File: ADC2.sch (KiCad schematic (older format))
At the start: 11 parts, among them U36 TLA2024IRUGR

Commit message: PVT
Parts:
- U56: renamed from U36; value TLA2024IRUGR -> ADS1015IDGSR; footprint IC-QFN:QFN10_1.5x2.0_P0.5_001 -> IC-SOP:VSSOP10_3.0x3.0_P0.5; symbol analog-ti:TLA2024 -> analog-ti:ADS1015; PartName TLA2024IRUGR -> ADS1015IDGSR
- renumbered C154 to C231, C155 to C232, C156 to C233, R92 to R119, R93 to R120, R94 to R121, R95 to R122, R96 to R123, TP31 to TP29, TP32 to TP30
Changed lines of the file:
@@
 $Descr A4 11693 8268
 encoding utf-8
-Sheet 18 24
-Title "Phoenix DVT"
-Date "2020-05-18"
+Sheet 24 24
+Title "Phoenix PVT"
+Date "2020-07-19"
 Rev "1"
 Comp ""
@@
 $EndDescr
 $Comp
-L analog-ti:TLA2024 U36
+L analog-ti:ADS1015 U56
 U 1 1 5E49C93C
 P 6000 4000
-F 0 "U36" H 6000 4650 50  0000 C CNN
-F 1 "TLA2024IRUGR" H 6000 3350 50  0000 C CNN
-F 2 "IC-QFN:QFN10_1.5x2.0_P0.5_001" H 6000 4000 50  0001 C CNN
+F 0 "U56" H 6000 4650 50  0000 C CNN
+F 1 "ADS1015IDGSR" H 6000 3350 50  0000 C CNN
+F 2 "IC-SOP:VSSOP10_3.0x3.0_P0.5" H 6000 4000 50  0001 C CNN
 F 3 "" H 6000 4000 50  0001 C CNN
-F 4 "TLA2024IRUGR" H 6000 4000 50  0001 C CNN "PartName"
+F 4 "ADS1015IDGSR" H 6000 4000 50  0001 C CNN "PartName"
 	1    6000 4000
 	1    0    0    -1
 $EndComp
 $Comp
-L passive:C C154
+L passive:C C231
 U 1 1 5E49D189
 P 5400 3700
-F 0 "C154" H 5500 3750 50  0000 L CNN
+F 0 "C231" H 5500 3750 50  0000 L CNN
 F 1 "100n" H 5500 3650 50  0000 L CNN
 F 2 "Capacitor-Chip:C_CHIP_1005_Hand_NoSilk" H 5500 3600 50  0001 C CNN
@@
 	7000 3400 7000 3700
 $Comp
-L supply-value:+3V3 #PWR0315
+L supply-value:+3V3 #PWR0438
 U 1 1 5E49DFE0
 P 6600 3200
-F 0 "#PWR0315" H 6600 3050 50  0001 C CNN
+F 0 "#PWR0438" H 6600 3050 50  0001 C CNN
 F 1 "+3V3" H 6600 3340 50  0000 C CNN
 F 2 "" H 6600 3200 50  0001 C CNN
@@
 $EndComp
 $Comp
-L supply-value:+3V3 #PWR0317
+L supply-value:+3V3 #PWR0440
 U 1 1 5E49E481
 P 7000 3200
-F 0 "#PWR0317" H 7000 3050 50  0001 C CNN
+F 0 "#PWR0440" H 7000 3050 50  0001 C CNN
 F 1 "+3V3" H 7000 3340 50  0000 C CNN
 F 2 "" H 7000 3200 50  0001 C CNN
@@
 $EndComp
 $Comp
-L supply-alias:GND #PWR0313
+L supply-alias:GND #PWR0436
 U 1 1 5E49E826
 P 5400 3900
-F 0 "#PWR0313" H 5400 3650 50  0001 C CNN
+F 0 "#PWR0436" H 5400 3650 50  0001 C CNN
 F 1 "GND" H 5400 3750 50  0000 C CNN
 F 2 "" H 5400 3900 50  0001 C CNN
@@
 	5400 3500 5600 3500
 $Comp
-L supply-alias:GND #PWR0314
+L supply-alias:GND #PWR0437
 U 1 1 5E4A0461
 P 5400 4500
-F 0 "#PWR0314" H 5400 4250 50  0001 C CNN
+F 0 "#PWR0437" H 5400 4250 50  0001 C CNN
 F 1 "GND" H 5400 4350 50  0000 C CNN
 F 2 "" H 5400 4500 50  0001 C CNN
@@
 CS-
 $Comp
-L supply-alias:GND #PWR0318
+L supply-alias:GND #PWR0441
 U 1 1 5E4A21A6
 P 7000 4900
-F 0 "#PWR0318" H 7000 4650 50  0001 C CNN
+F 0 "#PWR0441" H 7000 4650 50  0001 C CNN
 F 1 "GND" H 7000 4750 50  0000 C CNN
 F 2 "" H 7000 4900 50  0001 C CNN
@@
 	7400 4500 7400 4600
 $Comp
-L passive:C C155
+L passive:C C232
 U 1 1 5E4A2C50
 P 7000 4700
-F 0 "C155" H 7100 4750 50  0000 L CNN
+F 0 "C232" H 7100 4750 50  0000 L CNN
 F 1 "10n" H 7100 4650 50  0000 L CNN
 F 2 "Capacitor-Chip:C_CHIP_1005_Hand_NoSilk" H 7100 4600 50  0001 C CNN
@@
 $EndComp
 $Comp
-L passive:R R95
+L passive:R R122
 U 1 1 5E4A13E8
 P 7900 4500
-F 0 "R95" V 7800 4500 50  0000 C CNN
+F 0 "R122" V 7800 4500 50  0000 C CNN
 F 1 "100k" V 8000 4500 50  0000 C CNN
 F 2 "Resistor-Chip:R_CHIP_1005_Hand_NoSilk" V 7950 4400 50  0001 C CNN
@@
 $EndComp
 $Comp
-L supply-value:+48V #PWR0319
+L supply-value:+48V #PWR0442
 U 1 1 5E4A0E38
 P 8700 4500
-F 0 "#PWR0319" H 8700 4350 50  0001 C CNN
+F 0 "#PWR0442" H 8700 4350 50  0001 C CNN
 F 1 "+48V" H 8700 4640 50  0000 C CNN
 F 2 "" H 8700 4500 50  0001 C CNN
@@
 Connection ~ 7000 4900
 $Comp
-L passive:R R94
+L passive:R R121
 U 1 1 5E4A1DE3
 P 7400 4700
-F 0 "R94" H 7450 4750 50  0000 L CNN
+F 0 "R121" H 7450 4750 50  0000 L CNN
 F 1 "10k" H 7450 4650 50  0000 L CNN
 F 2 "Resistor-Chip:R_CHIP_1005_Hand_NoSilk" V 7450 4600 50  0001 C CNN
@@
 SDA
 $Comp
-L passive:C C156
+L passive:C C233
 U 1 1 5E5FCC2A
 P 7600 4000
-F 0 "C156" H 7700 4050 50  0000 L CNN
+F 0 "C233" H 7700 4050 50  0000 L CNN
 F 1 "100n" H 7700 3950 50  0000 L CNN
 F 2 "Capacitor-Chip:C_CHIP_1005_Hand_NoSilk" H 7700 3900 50  0001 C CNN
@@
 	6400 4100 7600 4100
 $Comp
-L passive:R R96
+L passive:R R123
 U 1 1 5F388480
 P 8400 4500
-F 0 "R96" V 8300 4500 50  0000 C CNN
+F 0 "R123" V 8300 4500 50  0000 C CNN
 F 1 "100k" V 8500 4500 50  0000 C CNN
 F 2 "Resistor-Chip:R_CHIP_1005_Hand_NoSilk" V 8450 4400 50  0001 C CNN
@@
 	6400 3900 7600 3900
 $Comp
-L supply-value:+3V3 #PWR0312
+L supply-value:+3V3 #PWR0435
 U 1 1 5EE44233
 P 5400 3500
-F 0 "#PWR0312" H 5400 3350 50  0001 C CNN
+F 0 "#PWR0435" H 5400 3350 50  0001 C CNN
 F 1 "+3V3" H 5400 3640 50  0000 C CNN
 F 2 "" H 5400 3500 50  0001 C CNN
@@
 Connection ~ 5400 3500
 $Comp
-L supply-alias:GND #PWR0316
+L supply-alias:GND #PWR0439
 U 1 1 5EEE5CDA
 P 6600 4500
-F 0 "#PWR0316" H 6600 4250 50  0001 C CNN
+F 0 "#PWR0439" H 6600 4250 50  0001 C CNN
 F 1 "GND" H 6600 4350 50  0000 C CNN
 F 2 "" H 6600 4500 50  0001 C CNN
@@
 	6400 3700 7000 3700
 $Comp
-L passive:R R92
+L passive:R R119
 U 1 1 5ED19405
 P 6600 3300
-F 0 "R92" H 6650 3350 50  0000 L CNN
+F 0 "R119" H 6650 3350 50  0000 L CNN
 F 1 "4.7k" H 6650 3250 50  0000 L CNN
 F 2 "Resistor-Chip:R_CHIP_1005_Hand_NoSilk" V 6650 3200 50  0001 C CNN
@@
 $EndComp
 $Comp
-L passive:R R93
+L passive:R R120
 U 1 1 5ED19765
 P 7000 3300
-F 0 "R93" H 7050 3350 50  0000 L CNN
+F 0 "R120" H 7050 3350 50  0000 L CNN
 F 1 "4.7k" H 7050 3250 50  0000 L CNN
 F 2 "Resistor-Chip:R_CHIP_1005_Hand_NoSilk" V 7050 3200 50  0001 C CNN
@@
 $EndComp
 $Comp
-L print:TestPoint TP31
+L print:TestPoint TP29
 U 1 1 5EF086EC
 P 7400 3400
-F 0 "TP31" H 7400 3700 50  0000 C CNN
+F 0 "TP29" H 7400 3700 50  0000 C CNN
 F 1 "SCL" H 7400 3600 50  0000 C CNN
 F 2 "Print:TP_C0.8" H 7100 3650 50  0001 C CNN
@@
 $EndComp
 $Comp
-L print:TestPoint TP32
+L print:TestPoint TP30
 U 1 1 5EF08F12
 P 7800 3400
-F 0 "TP32" H 7800 3700 50  0000 C CNN
+F 0 "TP30" H 7800 3700 50  0000 C CNN
 F 1 "SDA" H 7800 3600 50  0000 C CNN
 F 2 "Print:TP_C0.8" H 7500 3650 50  0001 C CNN

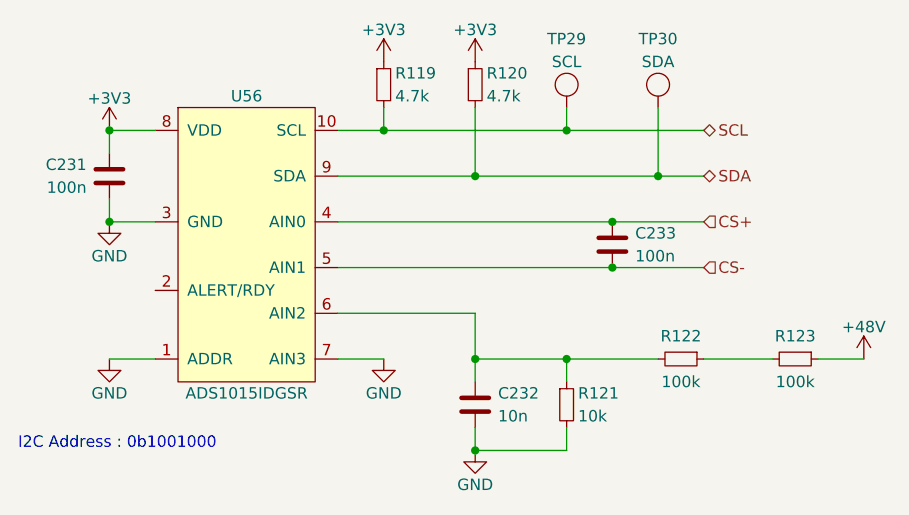
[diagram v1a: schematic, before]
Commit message: SBUにTVSダイオードを追加
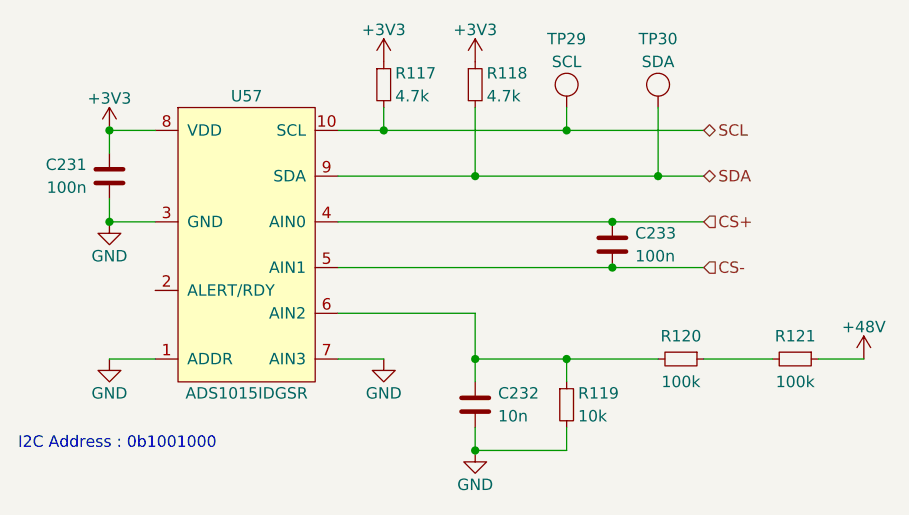
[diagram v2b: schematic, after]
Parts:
- renumbered R119 to R117, R120 to R118, R121 to R119, R122 to R120, R123 to R121, U56 to U57
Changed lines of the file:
@@
 $EndDescr
 $Comp
-L analog-ti:ADS1015 U56
+L analog-ti:ADS1015 U57
 U 1 1 5E49C93C
 P 6000 4000
-F 0 "U56" H 6000 4650 50  0000 C CNN
+F 0 "U57" H 6000 4650 50  0000 C CNN
 F 1 "ADS1015IDGSR" H 6000 3350 50  0000 C CNN
 F 2 "IC-SOP:VSSOP10_3.0x3.0_P0.5" H 6000 4000 50  0001 C CNN
@@
 $EndComp
 $Comp
-L passive:R R122
+L passive:R R120
 U 1 1 5E4A13E8
 P 7900 4500
-F 0 "R122" V 7800 4500 50  0000 C CNN
+F 0 "R120" V 7800 4500 50  0000 C CNN
 F 1 "100k" V 8000 4500 50  0000 C CNN
 F 2 "Resistor-Chip:R_CHIP_1005_Hand_NoSilk" V 7950 4400 50  0001 C CNN
@@
 Connection ~ 7000 4900
 $Comp
-L passive:R R121
+L passive:R R119
 U 1 1 5E4A1DE3
 P 7400 4700
-F 0 "R121" H 7450 4750 50  0000 L CNN
+F 0 "R119" H 7450 4750 50  0000 L CNN
 F 1 "10k" H 7450 4650 50  0000 L CNN
 F 2 "Resistor-Chip:R_CHIP_1005_Hand_NoSilk" V 7450 4600 50  0001 C CNN
@@
 	6400 4100 7600 4100
 $Comp
-L passive:R R123
+L passive:R R121
 U 1 1 5F388480
 P 8400 4500
-F 0 "R123" V 8300 4500 50  0000 C CNN
+F 0 "R121" V 8300 4500 50  0000 C CNN
 F 1 "100k" V 8500 4500 50  0000 C CNN
 F 2 "Resistor-Chip:R_CHIP_1005_Hand_NoSilk" V 8450 4400 50  0001 C CNN
@@
 	6400 3700 7000 3700
 $Comp
-L passive:R R119
+L passive:R R117
 U 1 1 5ED19405
 P 6600 3300
-F 0 "R119" H 6650 3350 50  0000 L CNN
+F 0 "R117" H 6650 3350 50  0000 L CNN
 F 1 "4.7k" H 6650 3250 50  0000 L CNN
 F 2 "Resistor-Chip:R_CHIP_1005_Hand_NoSilk" V 6650 3200 50  0001 C CNN
@@
 $EndComp
 $Comp
-L passive:R R120
+L passive:R R118
 U 1 1 5ED19765
 P 7000 3300
-F 0 "R120" H 7050 3350 50  0000 L CNN
+F 0 "R118" H 7050 3350 50  0000 L CNN
 F 1 "4.7k" H 7050 3250 50  0000 L CNN
 F 2 "Resistor-Chip:R_CHIP_1005_Hand_NoSilk" V 7050 3200 50  0001 C CNN
